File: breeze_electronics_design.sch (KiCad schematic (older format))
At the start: 100 parts, among them J1 SIP4, M1 Motor, M2 Motor, M3 Motor, M4 Motor, Q1 S8050, Q2 SI2303, Q3 SI2303, Q4 SI2303, Q5 SI2303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

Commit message: Modify the schematic of MCU
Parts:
- removed C1: 0.1UF, C0402, symbol Capacitance
- removed C2, C4: 2.2UF, C0402, symbol Capacitance
- removed J1: SIP4, symbol SIP4
- removed R1: 10K, R0402, symbol Resistor
- removed U1: STM32F103T8U6TR, symbol STM32F103T8U6TR
- removed Y1: 8MHZ, CSTCE8M00G55R0, symbol CrystalSMD
- added C?: 0.1UF, C_0402, symbol Capacitance
- added C? (x2): 2.2UF, C_0402, symbol Capacitance
- added J?: SIP4, Pin_Header_Straight_1x04, symbol SIP4
- added R?: 10K, R_0402, symbol Resistor
- added U?: STM32F103T8U6TR, VFQFPN_STM32F103T8U6TR, symbol STM32F103T8U6TR
- added Y?: 8MHZ, Resonator_7.2x3mm, symbol CrystalResonator
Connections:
- net labels removed: VCC+5V
- wire segments 402 -> 404

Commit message: Modify the schematic of LEDs
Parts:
- removed D3: M3_LED_TOP, LED0603, symbol Led
- removed LED1: POWER, LED0603, symbol Led
- removed LED10: CHG_LED, LED0603, symbol Led
- removed LED2: M1_LED_TOP, LED0603, symbol Led
- removed LED3: M1_LED_BOT, LED0603, symbol Led
- removed LED4: M2_LED_TOP, LED0603, symbol Led
- removed LED5: M2_LED_BOT, LED0603, symbol Led
- removed LED6: M3_LED_BOT, LED0603, symbol Led
- removed LED7: M4_LED_TOP, LED0603, symbol Led
- removed LED8: M4_LED_BOT, LED0603, symbol Led
- removed LED9: BT_LED, LED0603, symbol Led
- removed R10, R11, R12, R13, R14, R9: 100, R0402, symbol Resistor
- removed R8: 10K, R0402, symbol Resistor
- added LED?: M1_LED_TOP, LED_0603, symbol LED
- added LED?: M1_LED_BOT, LED_0603, symbol LED
- added LED?: M2_LED_TOP, LED_0603, symbol LED
- added LED?: M2_LED_BOT, LED_0603, symbol LED
- added LED?: M3_LED_TOP, LED_0603, symbol LED
- added LED?: M3_LED_BOT, LED_0603, symbol LED
- added LED?: M4_LED_TOP, LED_0603, symbol LED
- added LED?: M4_LED_BOT, LED_0603, symbol LED
- added LED?: POWER, LED_0603, symbol LED
- added LED?: BT_LED, LED_0603, symbol LED
- added LED?: CHG_LED, LED_0603, symbol LED
- added R? (x6): 100, R_0402, symbol Resistor
- added R?: 10K, R_0402, symbol Resistor

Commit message: Modify the schematic of Wireless
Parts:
- removed A1: Antenna, AN950-245, symbol Antenna
- removed C16, C26: 2.2UF, C0402, symbol Capacitance
- removed C17, C20: 22PF, C0402, symbol Capacitance
- removed C18: 2.2NF, C0402, symbol Capacitance
- removed C19: 4.7PF, C0402, symbol Capacitance
- removed C22: 1.5PF, C0402, symbol Capacitance
- removed C23: 1PF, C0402, symbol Capacitance
- removed C24: 0.1UF, C0402, symbol Capacitance
- removed L2: 8.2NH, L0402, symbol Inductor
- removed L3: 2.7NH, L0402, symbol Inductor
- removed L4: 3.9NH, L0402, symbol Inductor
- removed R19: 22K, R0402, symbol Resistor
- removed U7: NRF24L01, symbol NRF24L01
- removed U?: HM-06-BT, BT_UART_13D5X18D5MM, symbol HM-06-BT
- removed X1: 16MHZ, XTAL_32X25, symbol XTAL
- added ANT?: Antenna, SMD_AN9520, symbol Antenna
- added C? (x2): 2.2UF, C_0402, symbol Capacitance
- added C?: 1PF, C_0402, symbol Capacitance
- added C?: 1.5PF, C_0402, symbol Capacitance
- added C?: 4.7PF, C_0402, symbol Capacitance
- added C?: 2.2NF, C_0402, symbol Capacitance
- added C?: 0.1UF, C_0402, symbol Capacitance
- added C? (x2): 22PF, C_0402, symbol Capacitance
- added L?: 3.9NH, SMD_L0402, symbol Inductor
- added L?: 8.2NH, SMD_L0402, symbol Inductor
- added L?: 2.7NH, SMD_L0402, symbol Inductor
- added R?: 22K, R_0402, symbol Resistor
- added U?: NRF24L01, QFN_NRF24L01, symbol NRF24L01
- added U?: HM_Bluetooth, SMD_HM, symbol HM_Bluetooth
- added X?: 16MHZ, SMD_XTAL3225, symbol CrystalOscillator

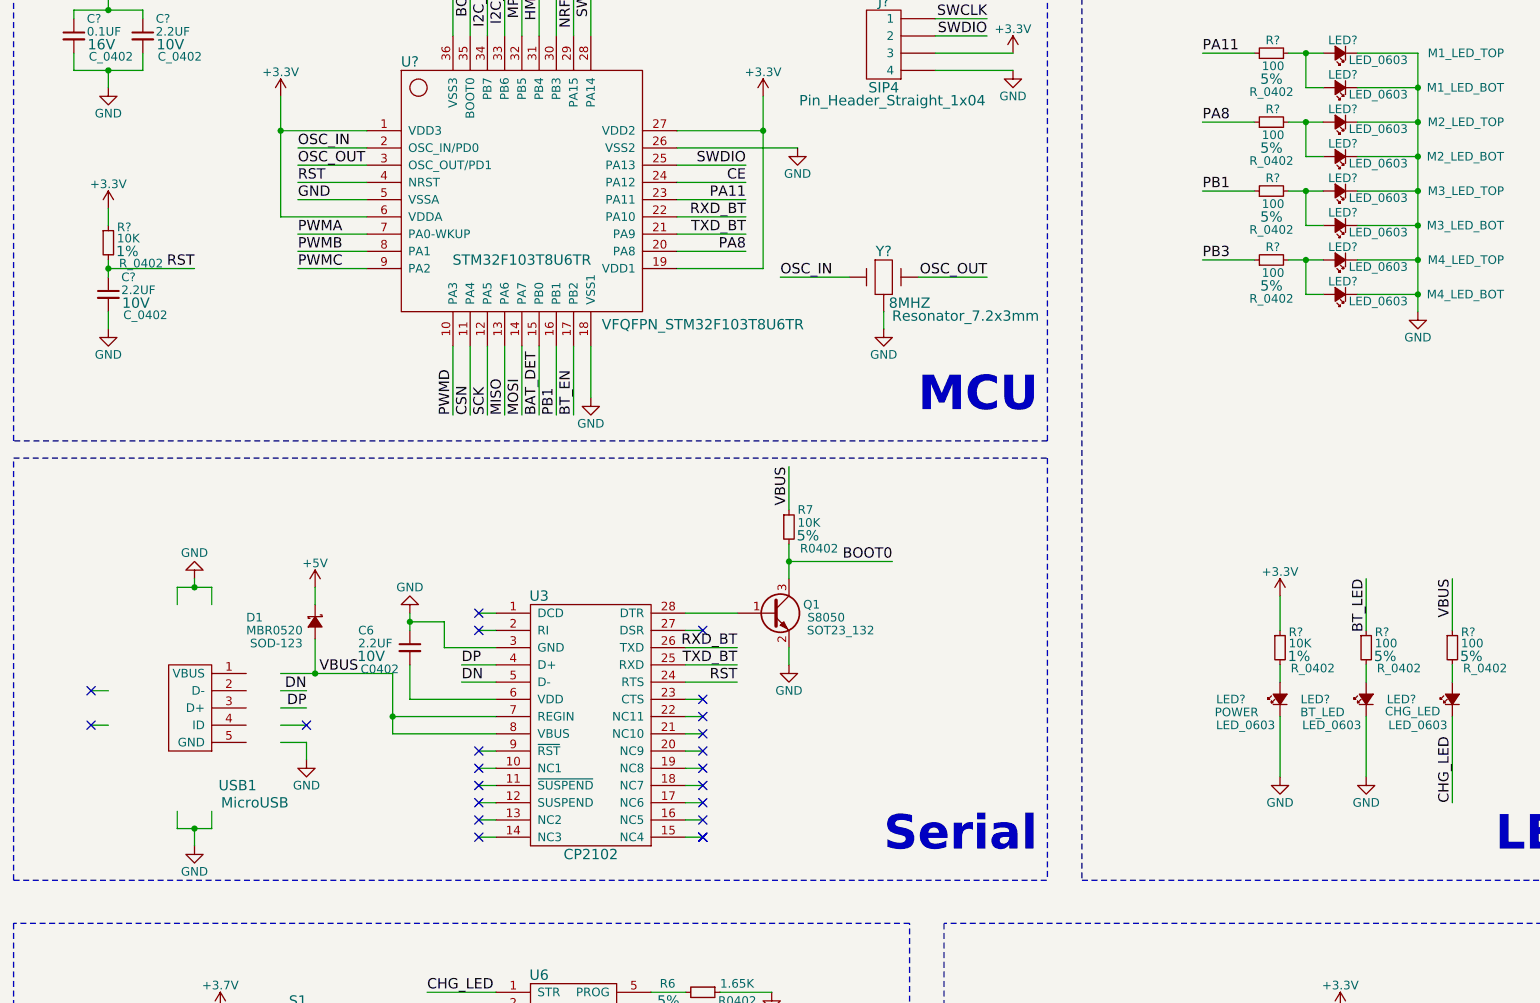
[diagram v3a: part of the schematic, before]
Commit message: Modify the schematic of Serial
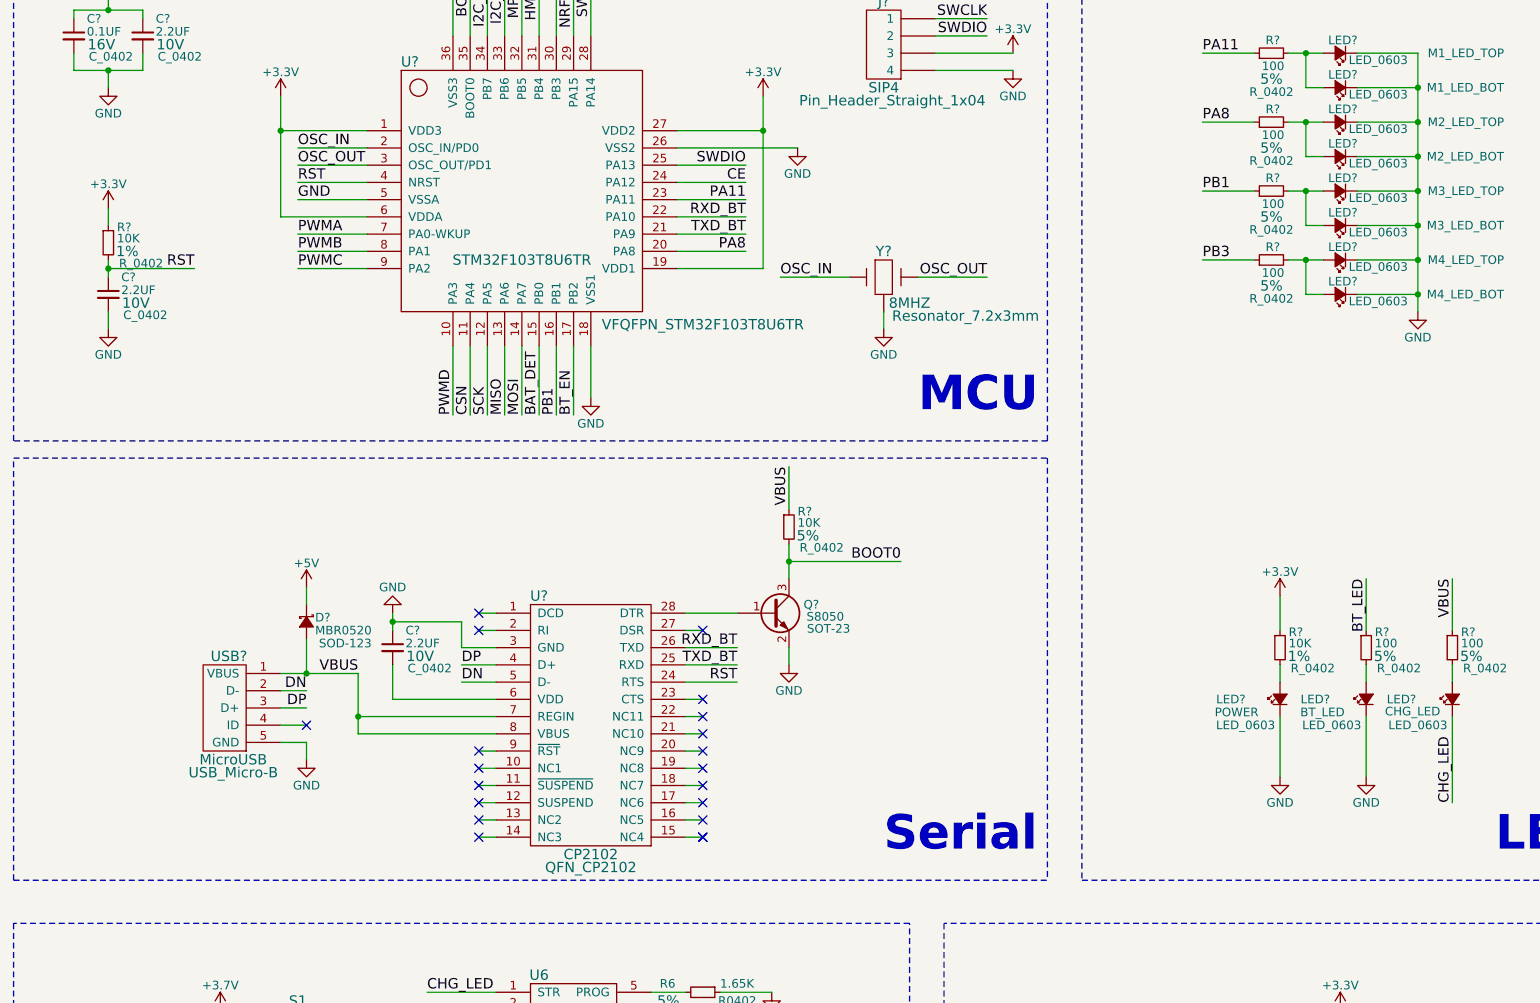
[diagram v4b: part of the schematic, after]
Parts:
- removed C6: 2.2UF, C0402, symbol Capacitance
- removed D1: MBR0520, SOD-123, symbol SchottkyDiode
- removed Q1: S8050, SOT23_132, symbol Triode
- removed R7: 10K, R0402, symbol Resistor
- removed U3: CP2102, symbol CP2102
- removed USB1: MicroUSB, symbol MicroUSB
- added C?: 2.2UF, C_0402, symbol Capacitance
- added D?: MBR0520, SOD-123, symbol SchottkyDiode
- added Q?: S8050, SOT-23, symbol Triode
- added R?: 10K, R_0402, symbol Resistor
- added U?: CP2102, QFN_CP2102, symbol CP2102
- added USB?: MicroUSB, USB_Micro-B, symbol MicroUSB
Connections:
- net BOOT0: now also Q?.3 (C), R?.2
- net DN: now also U?.5 (D-), USB?.2 (D-)
- net DP: now also U?.4 (D+), USB?.3 (D+)
- net RST: now also U?.24 (RTS)
- net RXD_BT: now also U?.26 (TXD)
- net TXD_BT: now also U?.25 (RXD)
- net VBUS: now also D?.2 (A), R?.1, U?.7 (REGIN), U?.8 (VBUS), USB?.1 (VBUS)
- new net: Q?.1 (B), U?.28 (DTR)
- new net: C?.1, U?.3 (GND)
- new net: C?.2, U?.6 (VDD)
- no-connect marks 50 -> 48

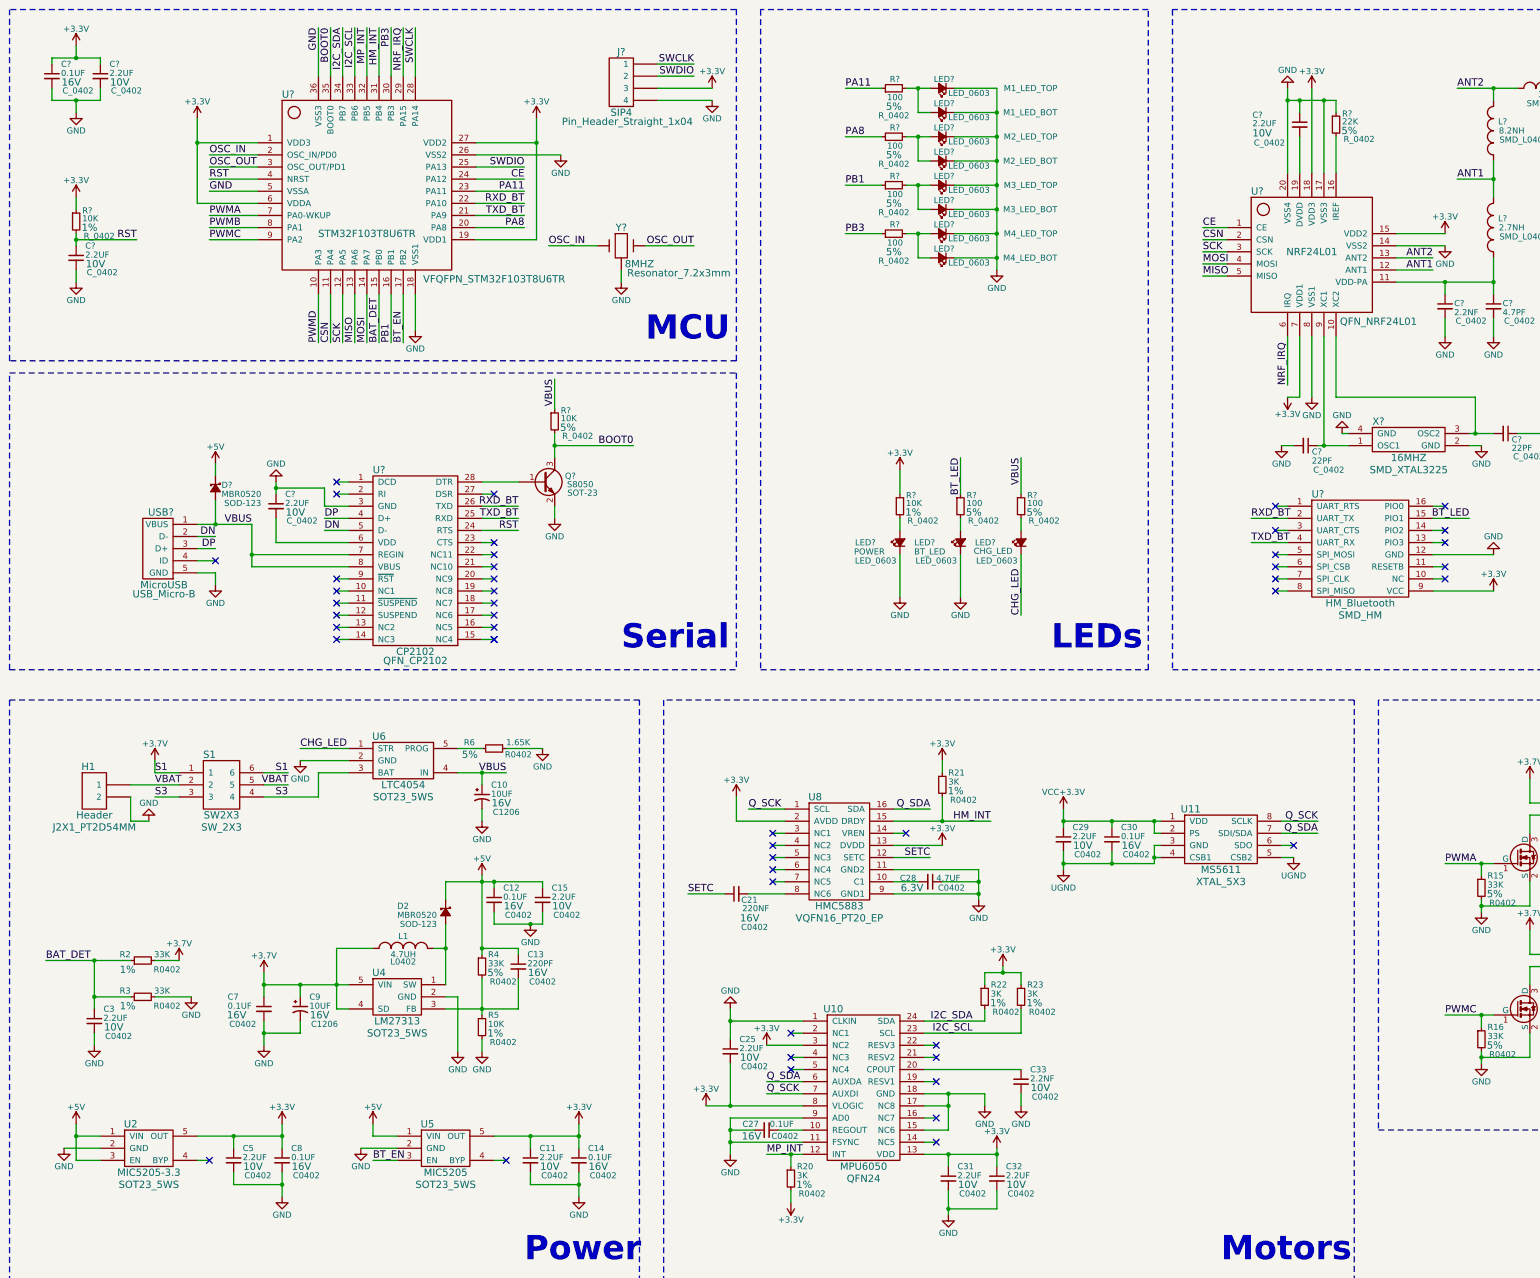
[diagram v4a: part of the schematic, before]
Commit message: Modify the schematic of Power
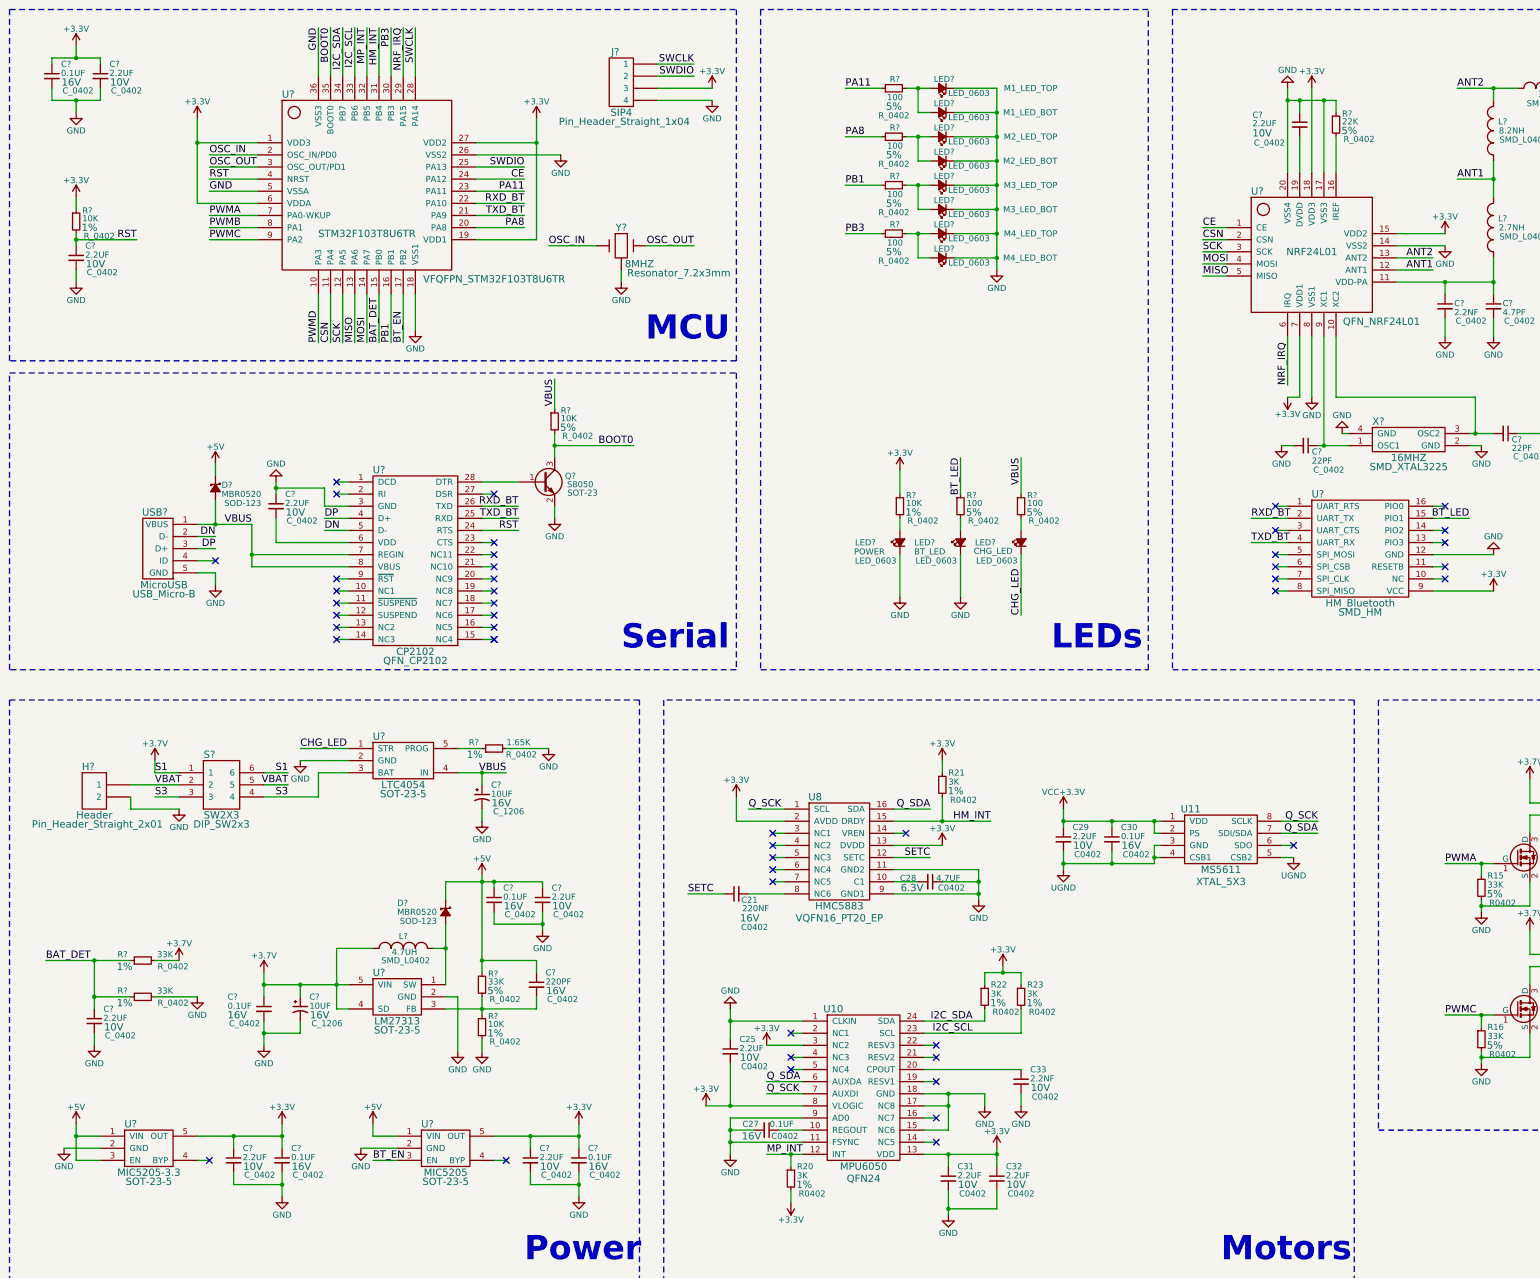
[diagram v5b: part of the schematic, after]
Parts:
- removed C10, C9: 10UF, C1206, symbol CapacitancePolar
- removed C11, C15, C3, C5: 2.2UF, C0402, symbol Capacitance
- removed C12, C14, C7, C8: 0.1UF, C0402, symbol Capacitance
- removed C13: 220PF, C0402, symbol Capacitance
- removed D2: MBR0520, SOD-123, symbol SchottkyDiode
- removed H1: Header, J2X1_PT2D54MM, symbol Header
- removed J?: SIP4, Pin_Header_Straight_1x04, symbol SIP4
- removed L1: 4.7UH, L0402, symbol Inductor
- removed R2, R3, R4: 33K, R0402, symbol Resistor
- removed R5: 10K, R0402, symbol Resistor
- removed R6: 1.65K, R0402, symbol Resistor
- removed S1: SW2X3, SW_2X3, symbol SW2X3
- removed U2: MIC5205-3.3, SOT23_5WS, symbol MIC5205-3.3
- removed U4: LM27313, SOT23_5WS, symbol LM27313
- removed U5: MIC5205, SOT23_5WS, symbol MIC5205
- removed U6: LTC4054, SOT23_5WS, symbol LTC4054
- removed U?: NRF24L01, QFN_NRF24L01, symbol NRF24L01
- removed U?: HM_Bluetooth, SMD_HM, symbol HM_Bluetooth
- removed USB?: MicroUSB, USB_Micro-B, symbol MicroUSB
- removed X?: 16MHZ, SMD_XTAL3225, symbol CrystalOscillator
- added C? (x2): 10UF, C_1206, symbol CapacitancePolar
- added C? (x4): 2.2UF, C_0402, symbol Capacitance
- added C? (x4): 0.1UF, C_0402, symbol Capacitance
- added C?: 220PF, C_0402, symbol Capacitance
- added D?: MBR0520, SOD-123, symbol SchottkyDiode
- added H?: Header, Pin_Header_Straight_2x01, symbol Header
- added J?: SIP4, Pin_Header_Straight_1x04, symbol SIP4
- added L?: 4.7UH, SMD_L0402, symbol Inductor
- added R?: 1.65K, R_0402, symbol Resistor
- added R? (x3): 33K, R_0402, symbol Resistor
- added R?: 10K, R_0402, symbol Resistor
- added S?: SW2X3, DIP_SW2x3, symbol SW2X3
- added U?: LM27313, SOT-23-5, symbol LM27313
- added U?: LTC4054, SOT-23-5, symbol LTC4054
- added U?: MIC5205-3.3, SOT-23-5, symbol MIC5205-3.3
- added U?: MIC5205, SOT-23-5, symbol MIC5205
- added U?: NRF24L01, QFN_NRF24L01, symbol NRF24L01
- added U?: HM_Bluetooth, SMD_HM, symbol HM_Bluetooth
- added USB?: MicroUSB, USB_Micro-B, symbol MicroUSB
- added X?: 16MHZ, SMD_XTAL3225, symbol CrystalOscillator
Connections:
- net ANT1: now also U?.12 (ANT1)
- net ANT2: now also U?.13 (ANT2)
- net BAT_DET: now also C?.1, R?.1, R?.1
- net BT_EN: now also U?.3 (EN)
- net BT_LED: now also U?.15 (PIO1)
- net CE: now also U?.1 (CE)
- net CHG_LED: now also U?.1 (STR)
- net CSN: now also U?.2 (CSN)
- net DN: now also USB?.2 (D-)
- net DP: now also USB?.3 (D+)
- net MISO: now also U?.5 (MISO)
- net MOSI: now also U?.4 (MOSI)
- net NRF_IRQ: now also U?.6 (IRQ)
- net RXD_BT: now also U?.2 (UART_TX)
- net S1: now also S?.1, S?.6
- net S3: now also S?.3, S?.4, U?.3 (BAT)
- net SCK: now also U?.3 (SCK)
- net SWCLK: now also J?.~ (4)
- net SWDIO: now also J?.~ (4)
- net TXD_BT: now also U?.4 (UART_RX)
- net VBAT: now also H?.~ (2), S?.2, S?.5
- net VBUS: now also C?.1, U?.4 (IN), USB?.1 (VBUS)
- net at C?.2: now also U?.10 (XC2), X?.3 (OSC2)
- net at C?.1, C?.1, L?.1: now also U?.11 (VDD-PA)
- net at R?.2: now also U?.16 (IREF)
- net at C?.1, R?.1: now also U?.17 (VSS3), U?.20 (VSS4)
- net at C?.2: now also U?.19 (DVDD)
- net at C?.1: now also U?.9 (XC1), X?.1 (OSC1)
- new net: R?.1, U?.5 (PROG)
- new net: C?.1, C?.1, L?.1, U?.4 (SD), U?.5 (VIN)
- new net: C?.2, C?.2 (x4)
- new net: D?.2 (A), L?.2, U?.1 (SW)
- new net: C?.2, R?.1, R?.2, U?.3 (FB)
- new net: C?.1, C?.1, C?.1, D?.1 (K), R?.1
- new net: C?.1, C?.1, U?.5 (OUT) (x2)
- new net: U?.1 (VIN), U?.3 (EN)
